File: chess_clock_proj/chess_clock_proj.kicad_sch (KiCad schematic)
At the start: 40 parts, among them J1 USB_A, J2 Conn_01x04_Male, J3 Conn_01x04_Male, J4 Conn_01x02, SW1 SW_SPDT, SW2 SW_Push, SW3 SW_Push, SW4 SW_Push, SW5 SW_Push, SW6 SW_Push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

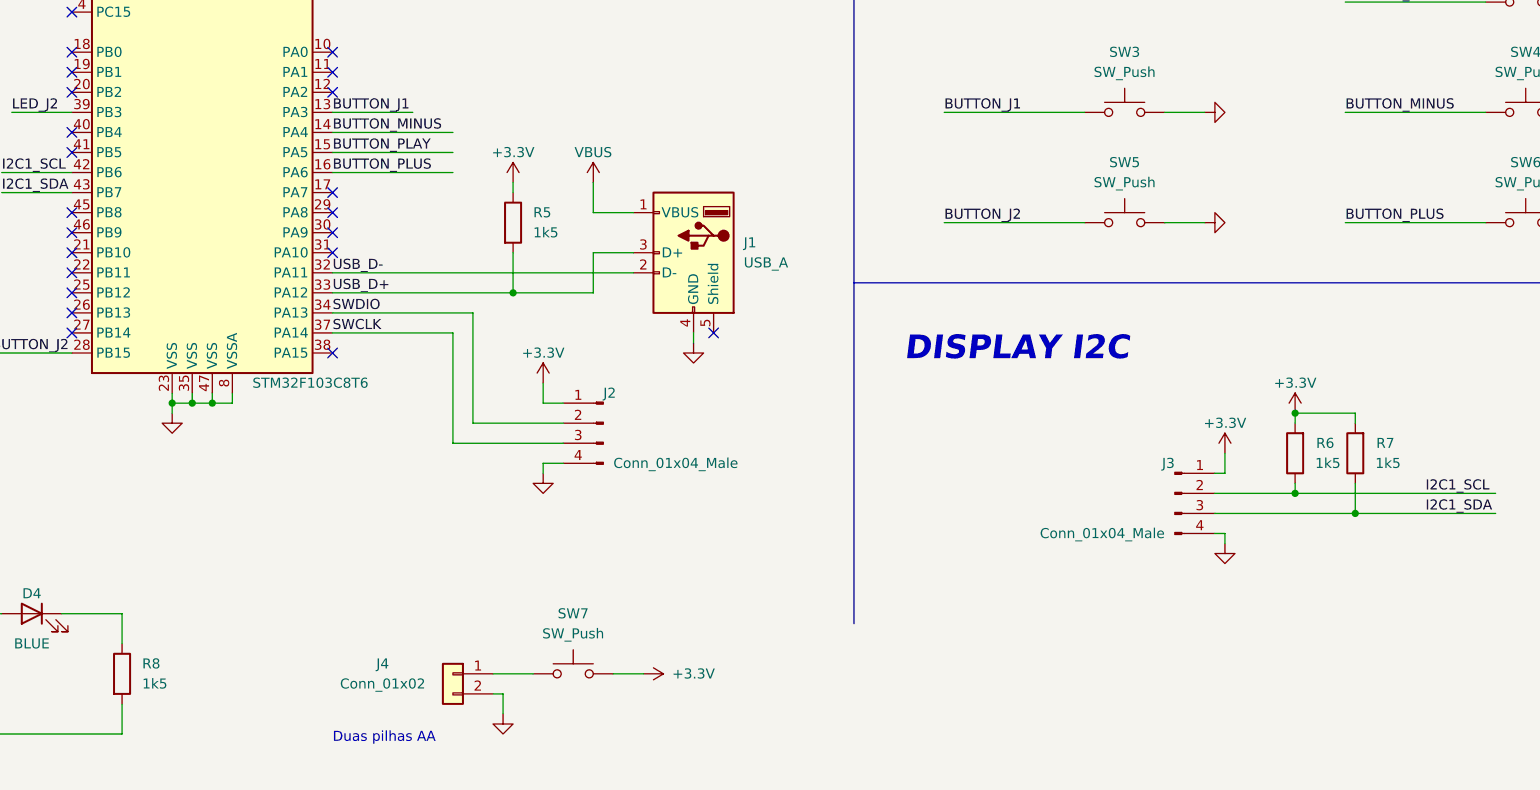
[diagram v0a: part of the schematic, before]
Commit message: alterei a posição da malha de terra, e retirei o resistor próximo ao USB
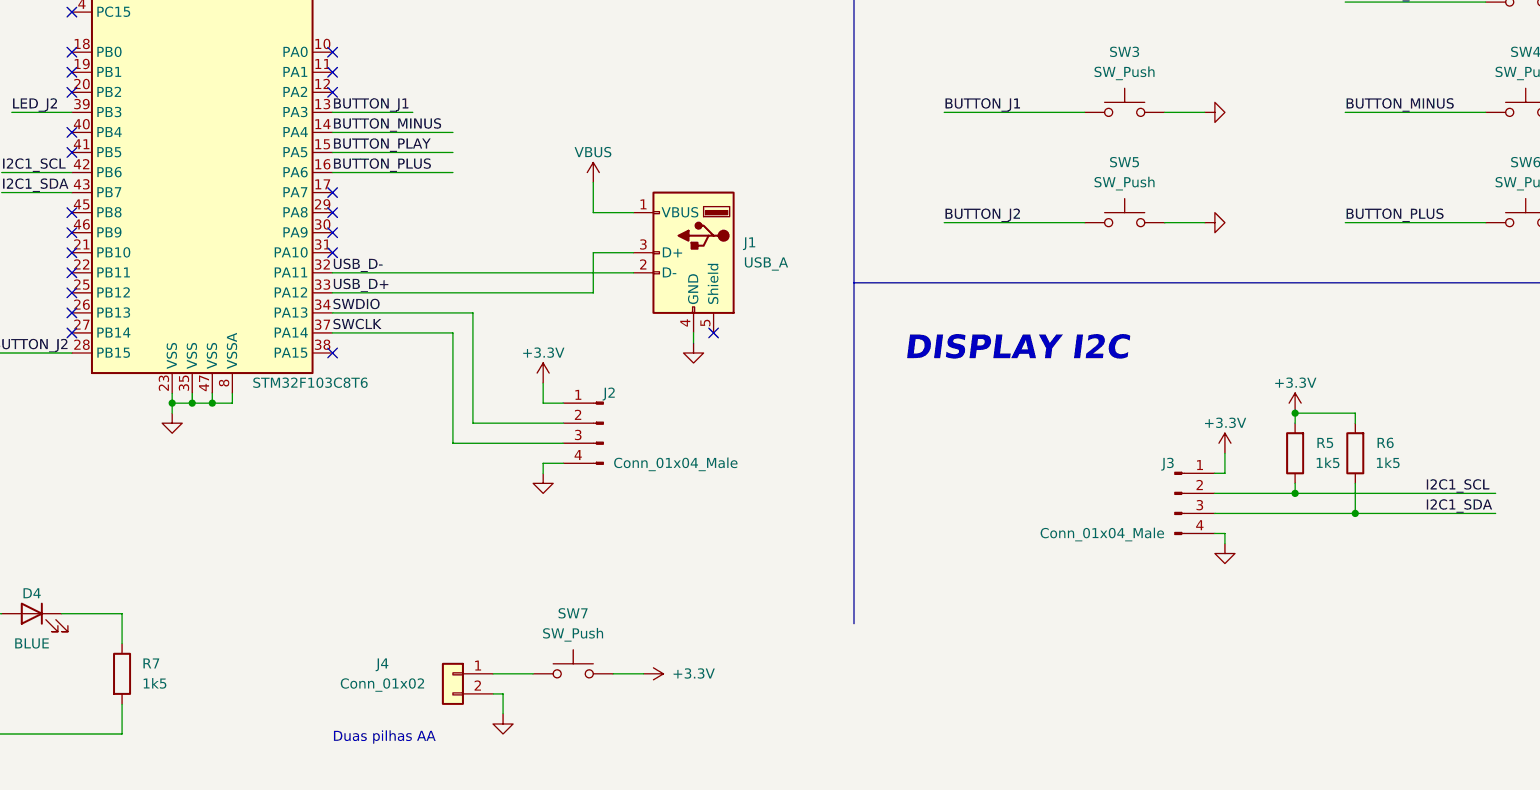
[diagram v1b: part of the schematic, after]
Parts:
- removed R5: 1k5, Resistor_SMD:R_0402_1005Metric, symbol Device:R
- renumbered R6 to R5, R7 to R6, R8 to R7
